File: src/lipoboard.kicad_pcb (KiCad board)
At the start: 2 copper layers, 41.9 x 32.5 mm, 50 parts, among them J1 USB_C_Receptacle_PowerOnly_24P, SW1 SW_DIP_x01, U1 TPS2116DRL, U2 TP4056, U3 DW01A, U4 TP5188, U5 TPS63001, U6 8025A

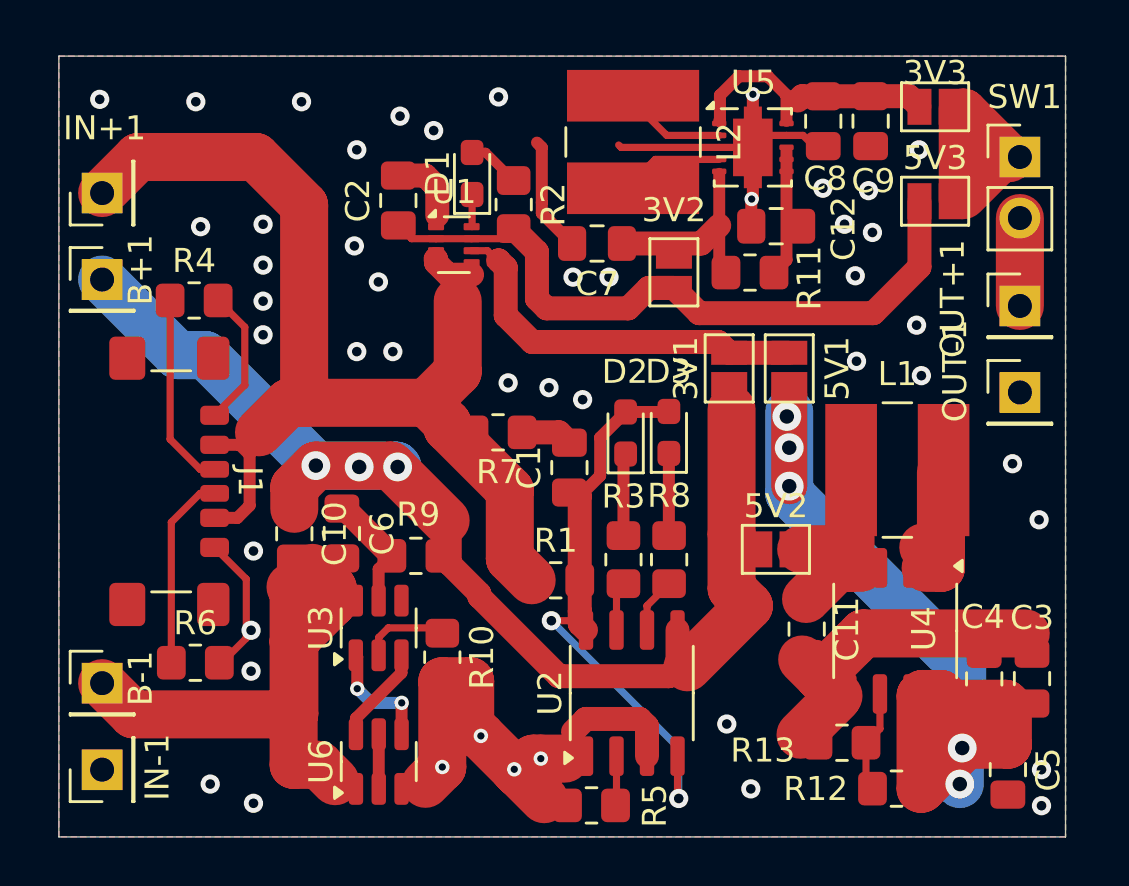
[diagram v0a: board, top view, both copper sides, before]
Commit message: Change dir structure
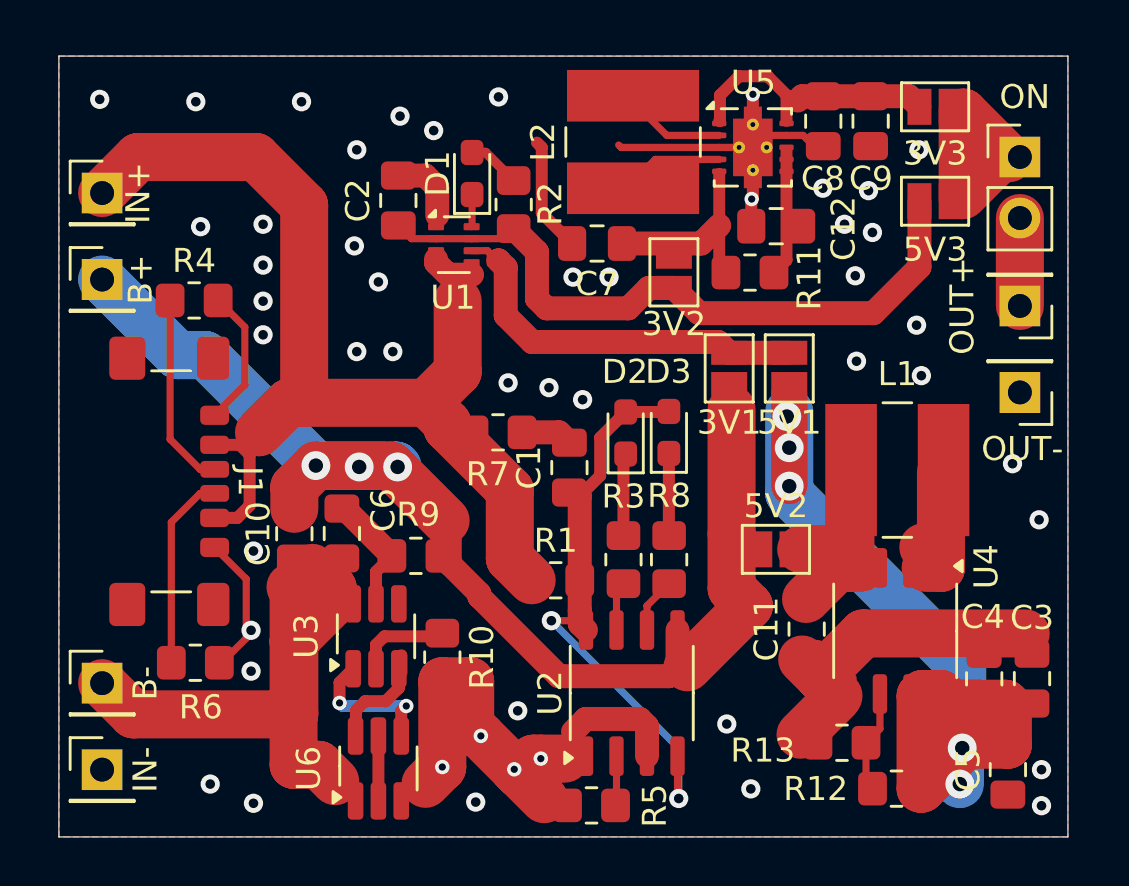
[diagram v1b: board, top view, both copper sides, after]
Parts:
- U3, U6: footprint Package_TO_SOT_SMD:SOT-23-6 -> Package_TO_SOT_SMD:SOT-23-6_Handsoldering
- U5: footprint Package_SON:Texas_DRC0010J -> Package_SON:Texas_DRC0010J_ThermalVias
- moved U3 0.36 mm to (72.6, 133.7)
- moved U6 0.29 mm to (72.7, 139.2)
- turned IN+ to 0 degrees
- turned IN- to 0 degrees
- turned OUT+ to 180 degrees
- turned OUT- to 180 degrees
- renumbered B+1 to B+, B-1 to B-, IN+1 to IN+, IN-1 to IN-, SW1 to ON, OUT+1 to OUT+, OUT-1 to OUT-
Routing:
- net Net-(U3-OD): track 4.82 -> 5.82 mm
- net Net-(U3-CS): track 3.65 -> 4.27 mm
- net Net-(U3-OC): track 4.07 -> 4.69 mm
- net GND: vias 47 -> 49
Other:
- board size 41.9 x 32.5 mm -> 42 x 32.5 mm
